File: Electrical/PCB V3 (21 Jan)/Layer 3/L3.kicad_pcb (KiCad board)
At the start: 2 copper layers, 129.9 x 110 mm, 28 parts, among them J1 Conn_01x06, J2 Conn_02x04_Odd_Even, J3 Conn_01x06, J4 Conn_01x06, J5 Conn_01x06, U2 113991054, U3 4754

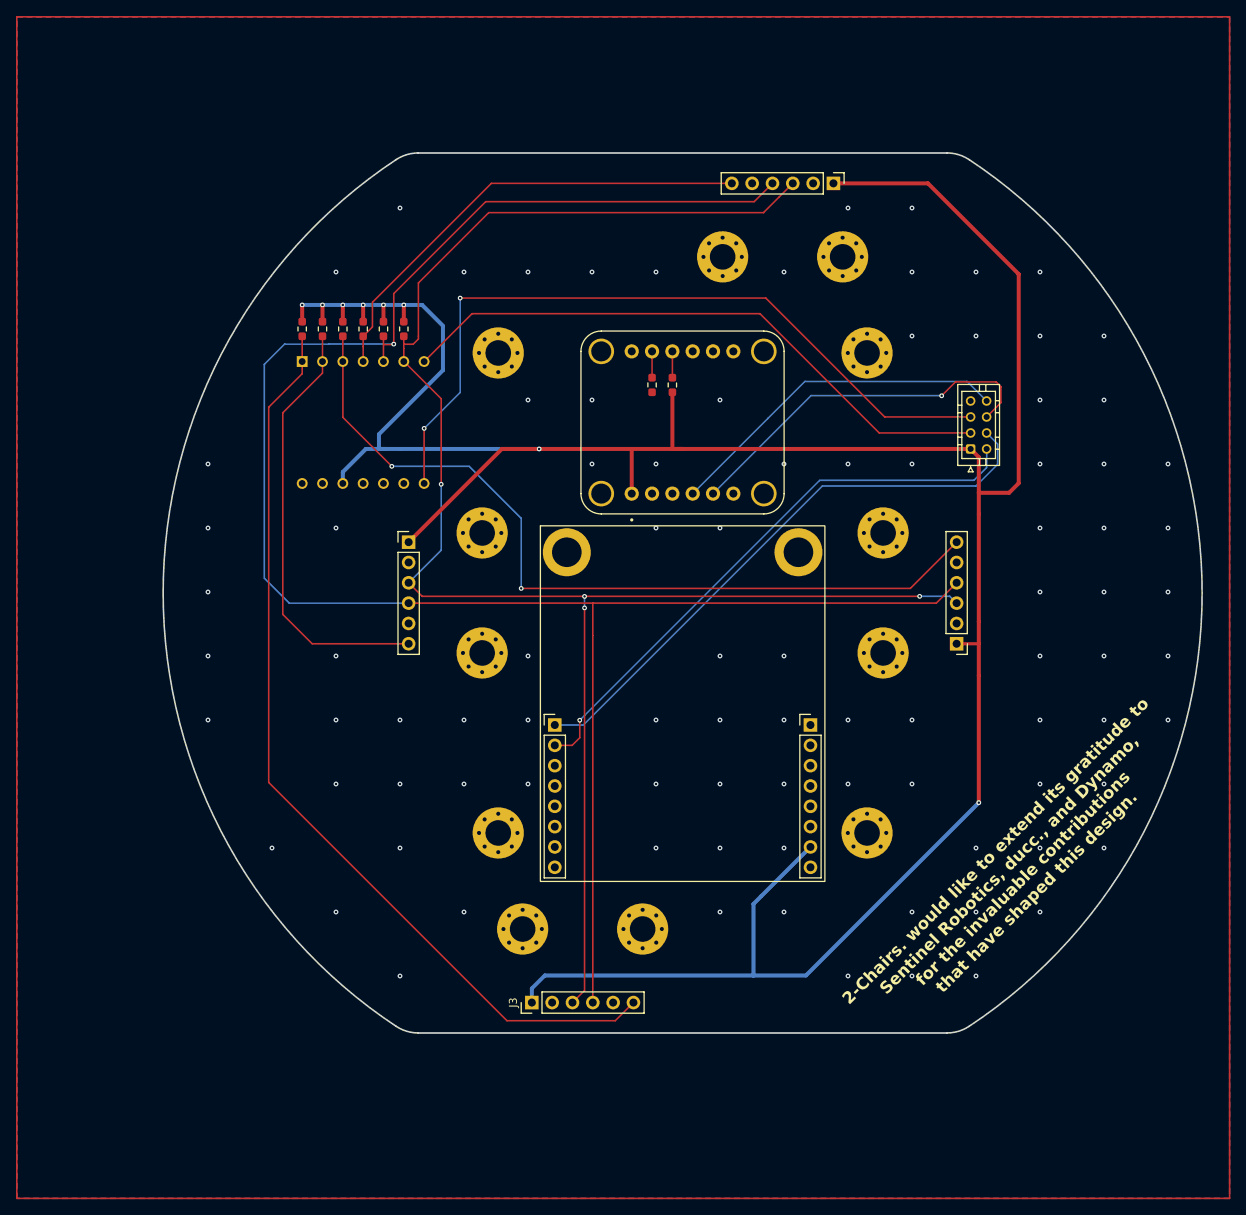
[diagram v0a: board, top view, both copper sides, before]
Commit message: fixed l1 and l3
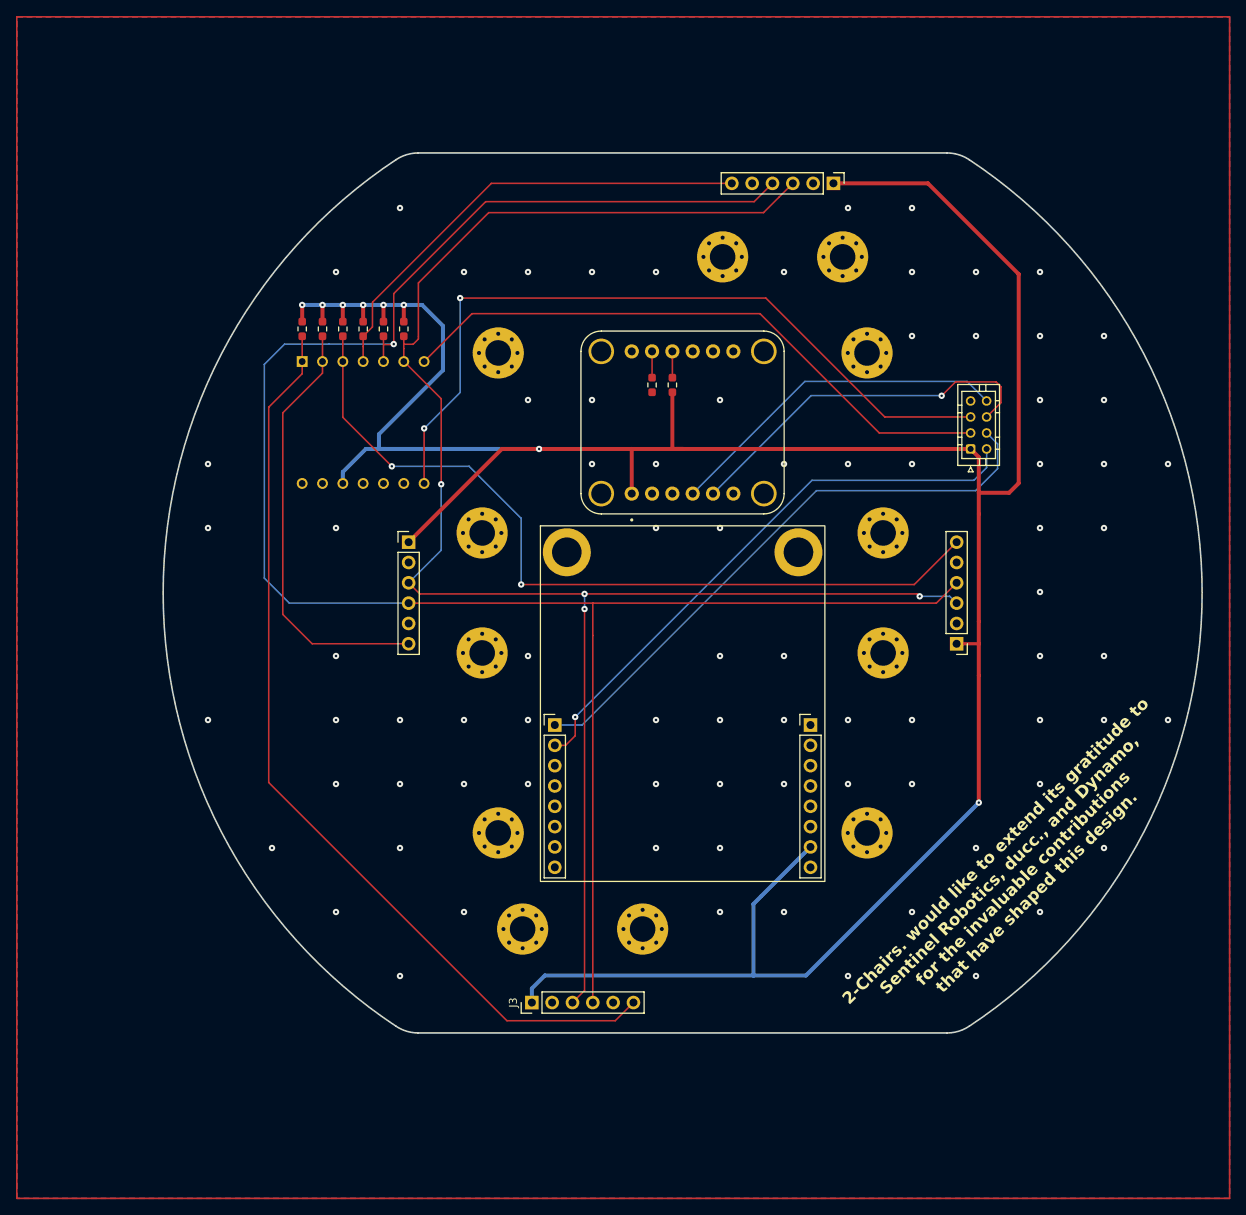
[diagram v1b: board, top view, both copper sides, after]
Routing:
- net /TOF3 XSHUT: track 103.2 -> 102.6 mm
- net GND: vias 92 -> 81

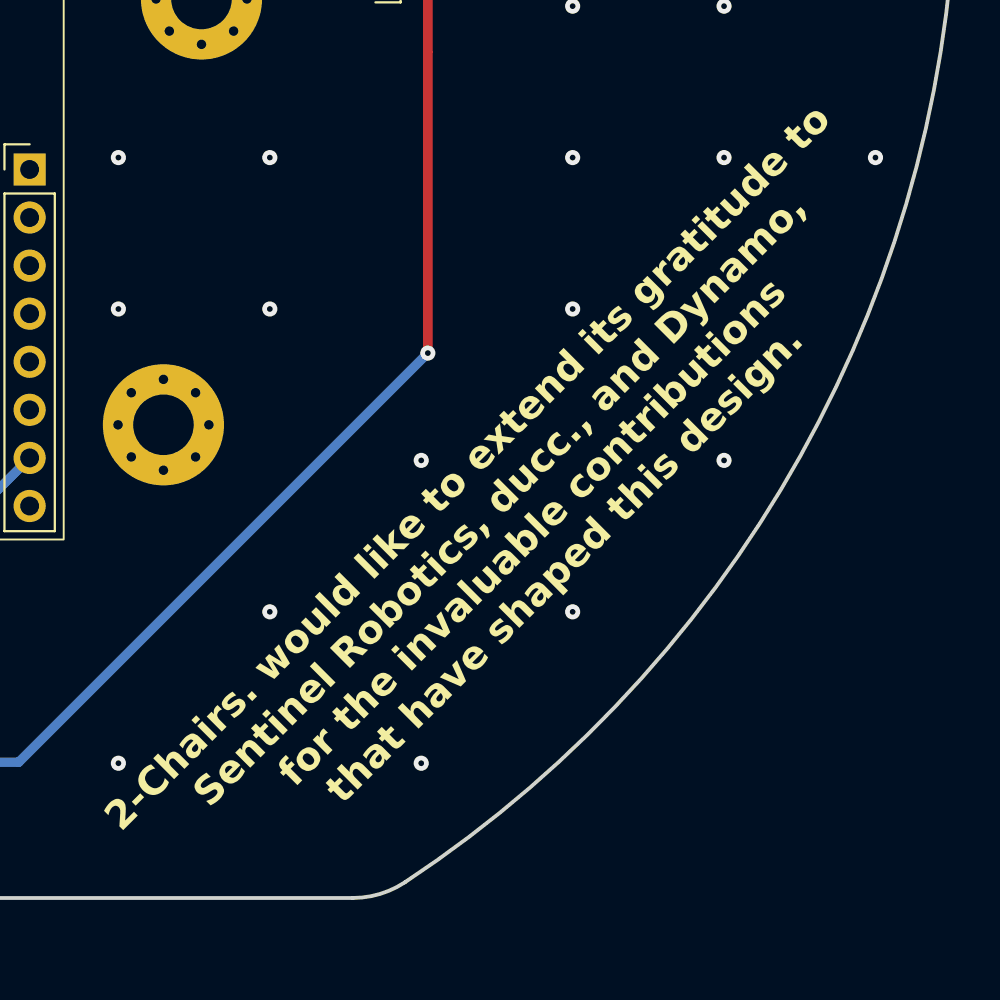
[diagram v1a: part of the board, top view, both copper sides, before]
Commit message: fixed l1 boost, started on activation circuit
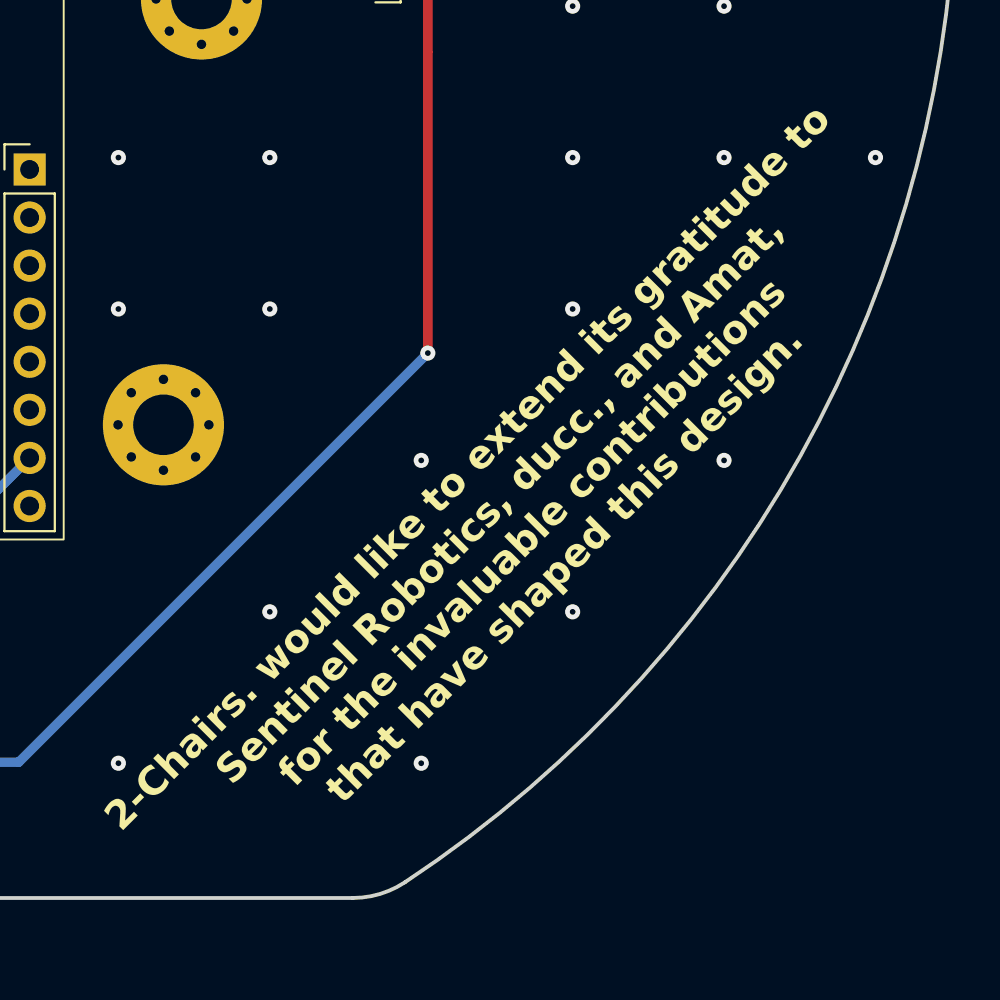
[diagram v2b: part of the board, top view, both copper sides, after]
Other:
- board text added: "2-Chairs. would like to extend its gratitude to Sentinel Robotics, ducc., and Amat, for the invaluable contributions that have shaped this design."
- board text removed: "2-Chairs. would like to extend its gratitude to Sentinel Robotics, ducc., and Dynamo, for the invaluable contributions that have shaped this design."
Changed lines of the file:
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@@
 		)
 	)
-	(gr_text "2-Chairs. would like to extend its gratitude to \nSentinel Robotics, ducc., and Dynamo, \nfor the invaluable contributions \nthat have shaped this design."
+	(gr_text "2-Chairs. would like to extend its gratitude to \nSentinel Robotics, ducc., and Amat, \nfor the invaluable contributions \nthat have shaped this design."
 		(at 255.410001 122.340001 45)
 		(layer "F.SilkS")

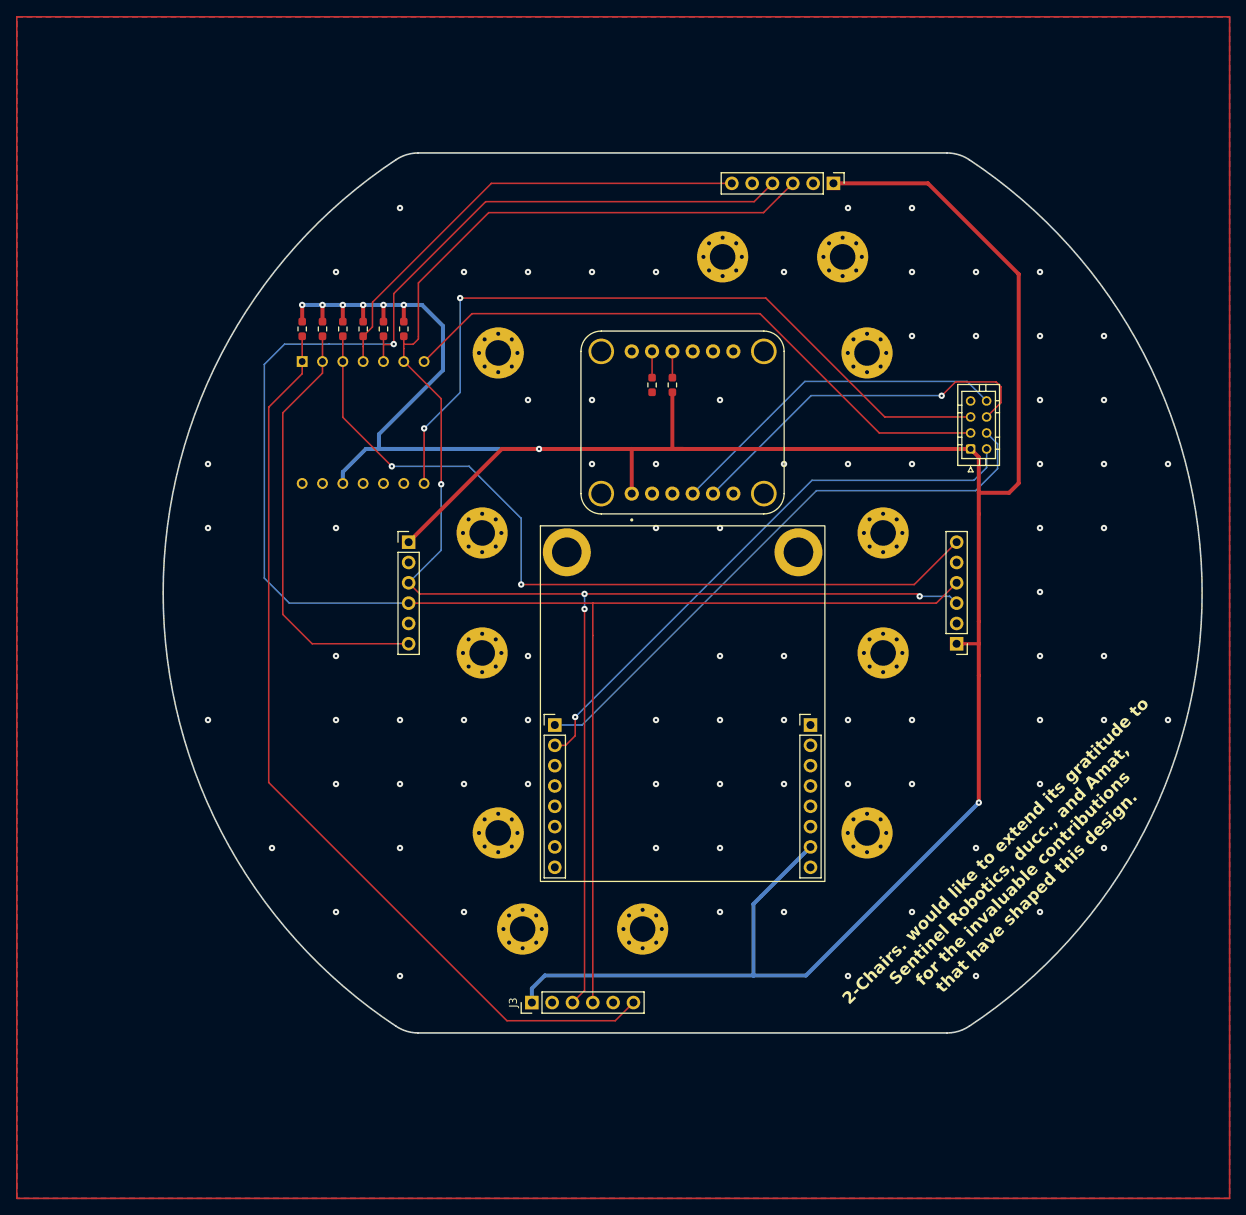
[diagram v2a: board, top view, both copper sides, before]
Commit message: fixed diode and activation cirucit for solenoid (l1), exported step files of all layers
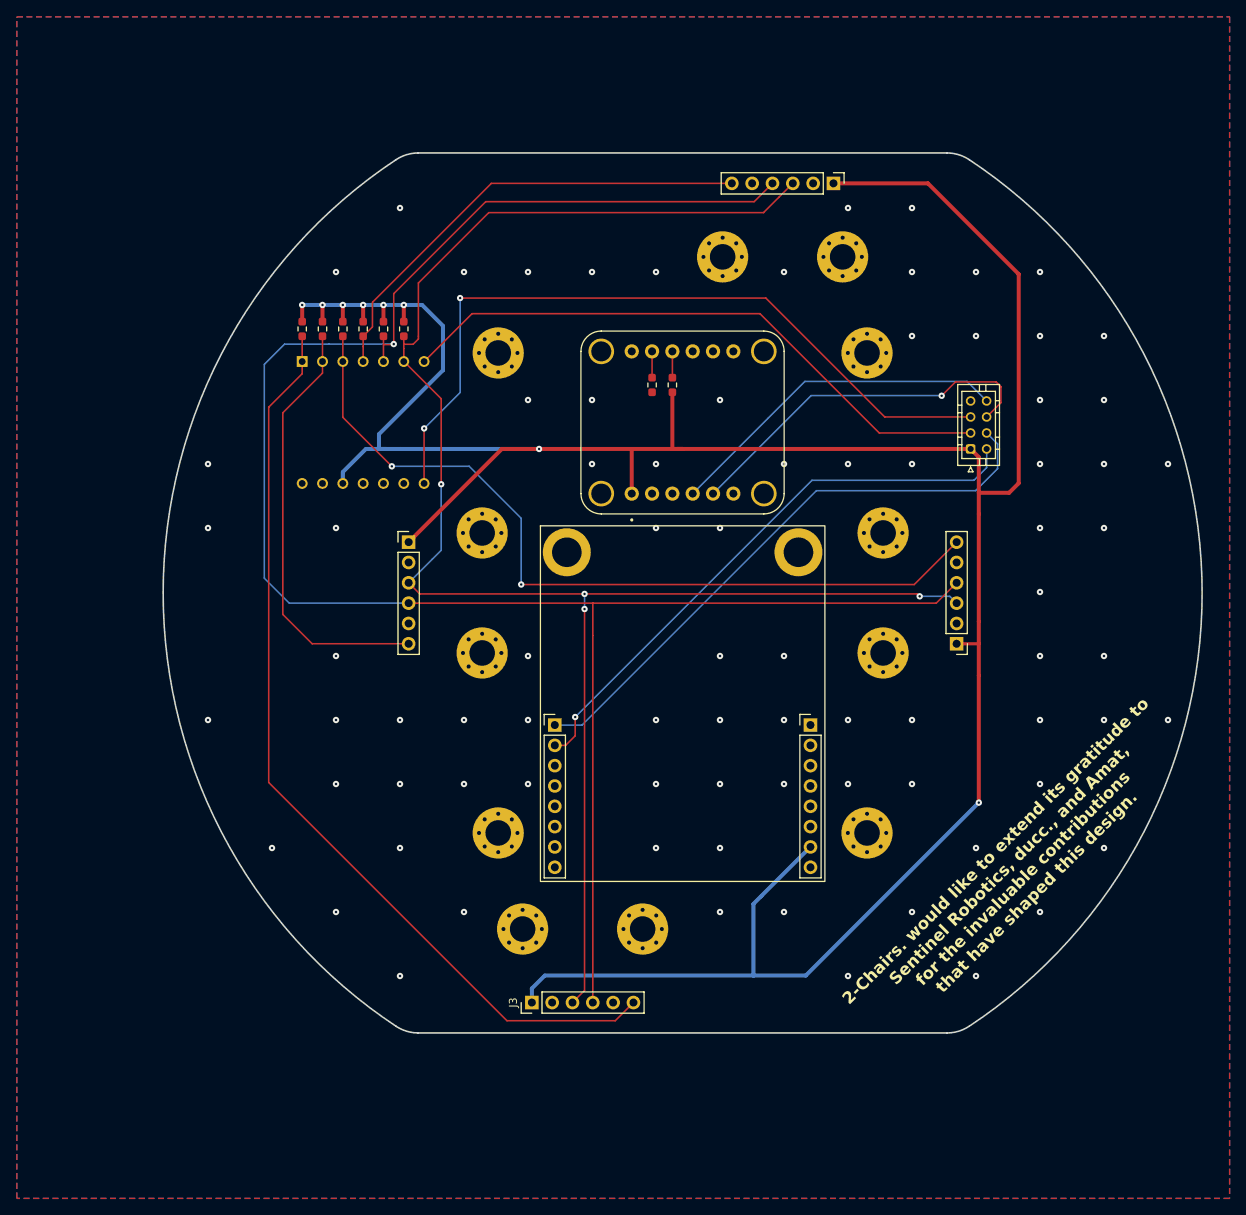
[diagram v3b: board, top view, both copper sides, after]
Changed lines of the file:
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@@
 		)
-	)
-	(gr_rect
-		(start 130.510001 15.510001)
-		(end 282.110001 163.210001)
-		(stroke
-			(width 0.2)
-			(type default)
-		)
-		(fill none)
-		(layer "F.Cu")
 	)
 	(gr_poly

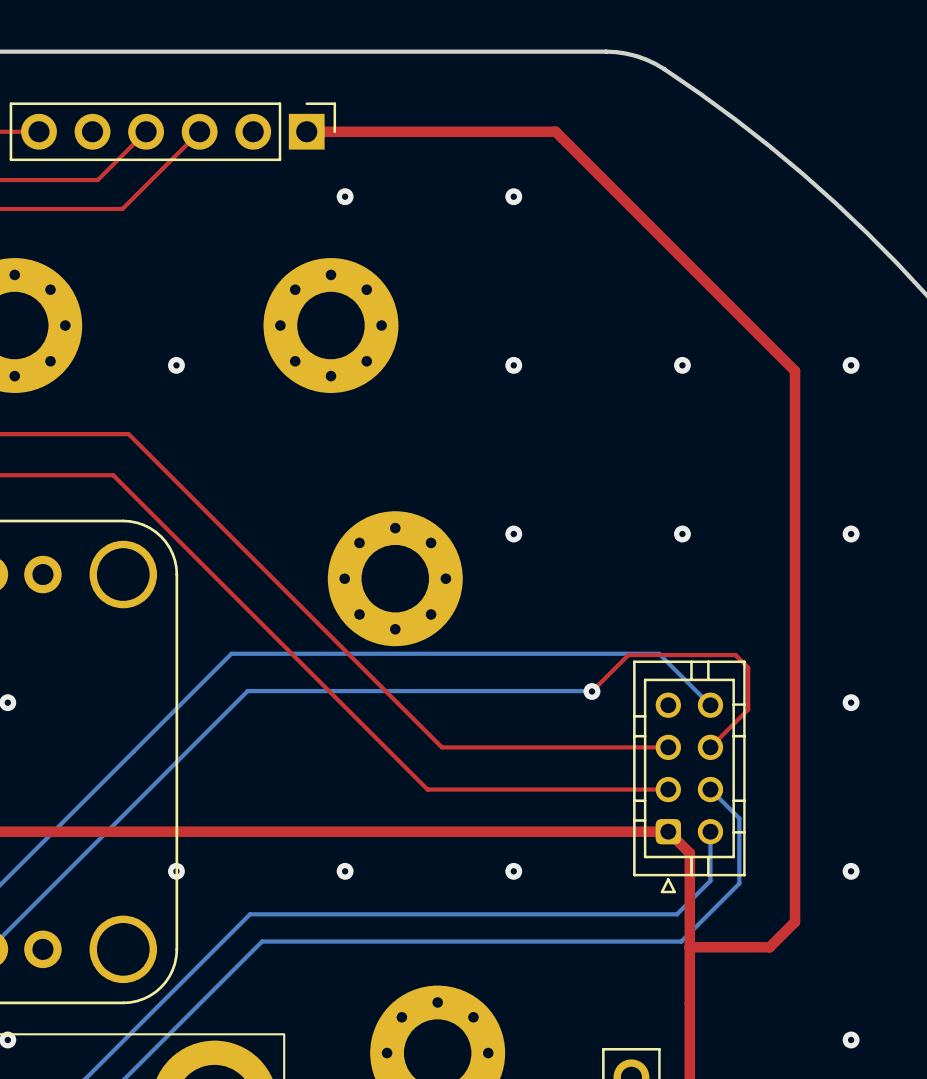
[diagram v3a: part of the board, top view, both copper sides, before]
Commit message: switched l3 jst
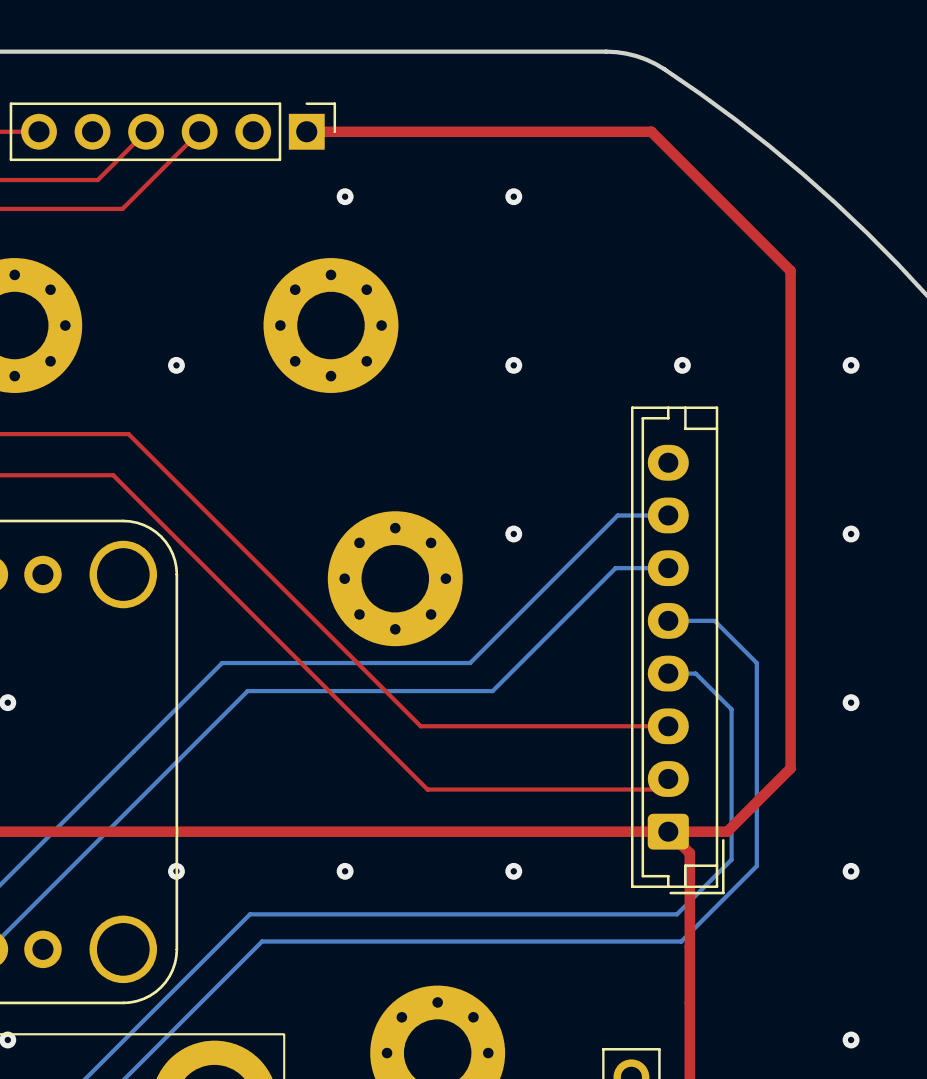
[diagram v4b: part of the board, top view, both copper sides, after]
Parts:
- J2: footprint Connector_JST:JST_PHD_B8B-PHDSS_2x04_P2.00mm_Vertical -> Connector_JST:JST_EH_B8B-EH-A_1x08_P2.50mm_Vertical
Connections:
- J2 pad 2: /TX (CAM) -> /TX (L3 ESP32)
- J2 pad 3: /TX (L3 ESP32) -> /RX (L3 ESP32)
- J2 pad 4: /RX (CAM) -> /TX (CAM)
- J2 pad 5: /RX (L3 ESP32) -> /RX (CAM)
- J2 pad 7: GND -> /RX (IMU)
- J2 pad 8: /RX (IMU) -> GND
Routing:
- net /RX (CAM): track 73.7 -> 84.5 mm
- net /TX (CAM): track 72.6 -> 82.5 mm
- net /TX (IMU): track 46.6 -> 39.7 mm, vias 1 -> 0
- net +3V3: track 361.1 -> 357.9 mm
- net GND: vias 81 -> 80
